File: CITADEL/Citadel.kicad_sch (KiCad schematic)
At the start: 33 parts, among them J1 Conn_01x02_Socket, J2 Conn_01x02_Socket, J3 USB3_A, J4 Conn_01x04_Socket, J5 Conn_01x03_Socket, J6 Conn_01x03_Socket, J7 Conn_01x03_Socket, J8 Conn_01x02_Pin, M1 Motor_DC, M2 Motor_DC, M3 Motor_DC, M4 Motor_DC, M5 Fan_Tacho, M6 Fan_Tacho, M7 Fan_Tacho, Q1 SSM3K329R_LF, Q2 SSM3K329R_LF, Q3 SSM3K329R_LF, Q4 SSM3K329R_LF, Q5 SSM3K329R_LF, Q6 SSM3K329R_LF, Q7 SSM3K329R_LF, U1 DEV-16771

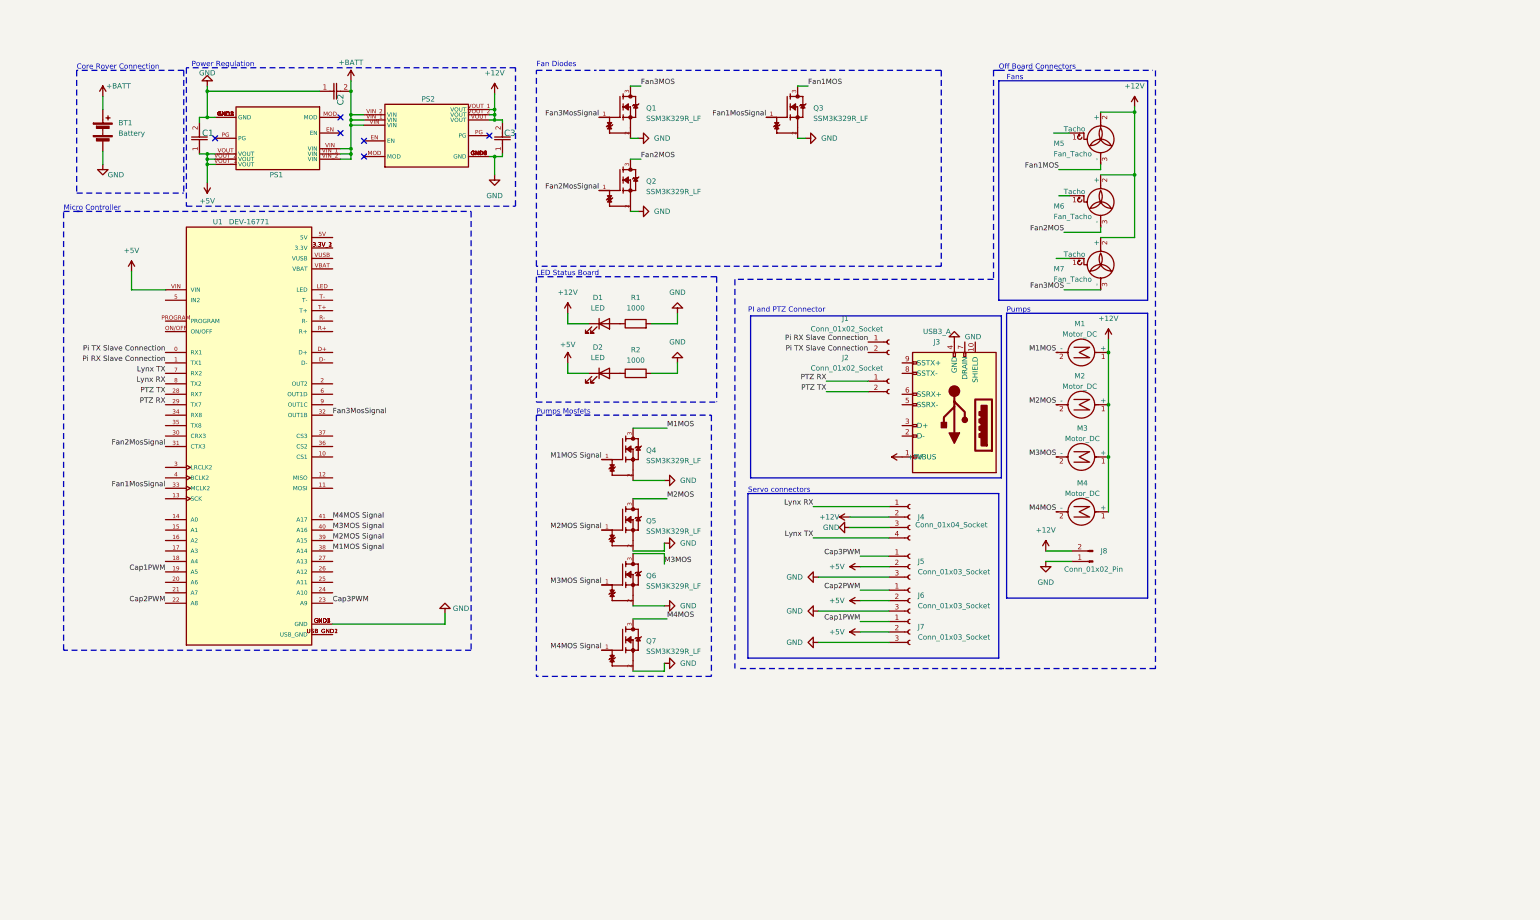
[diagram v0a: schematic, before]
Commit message: CITADEL 2025 V1, FAERIE 2025 V1
CITADEL January 27, 2025; FAERIE January 26, 2025; Katherine and Mason did CITADEL, Reymund did FAERIE
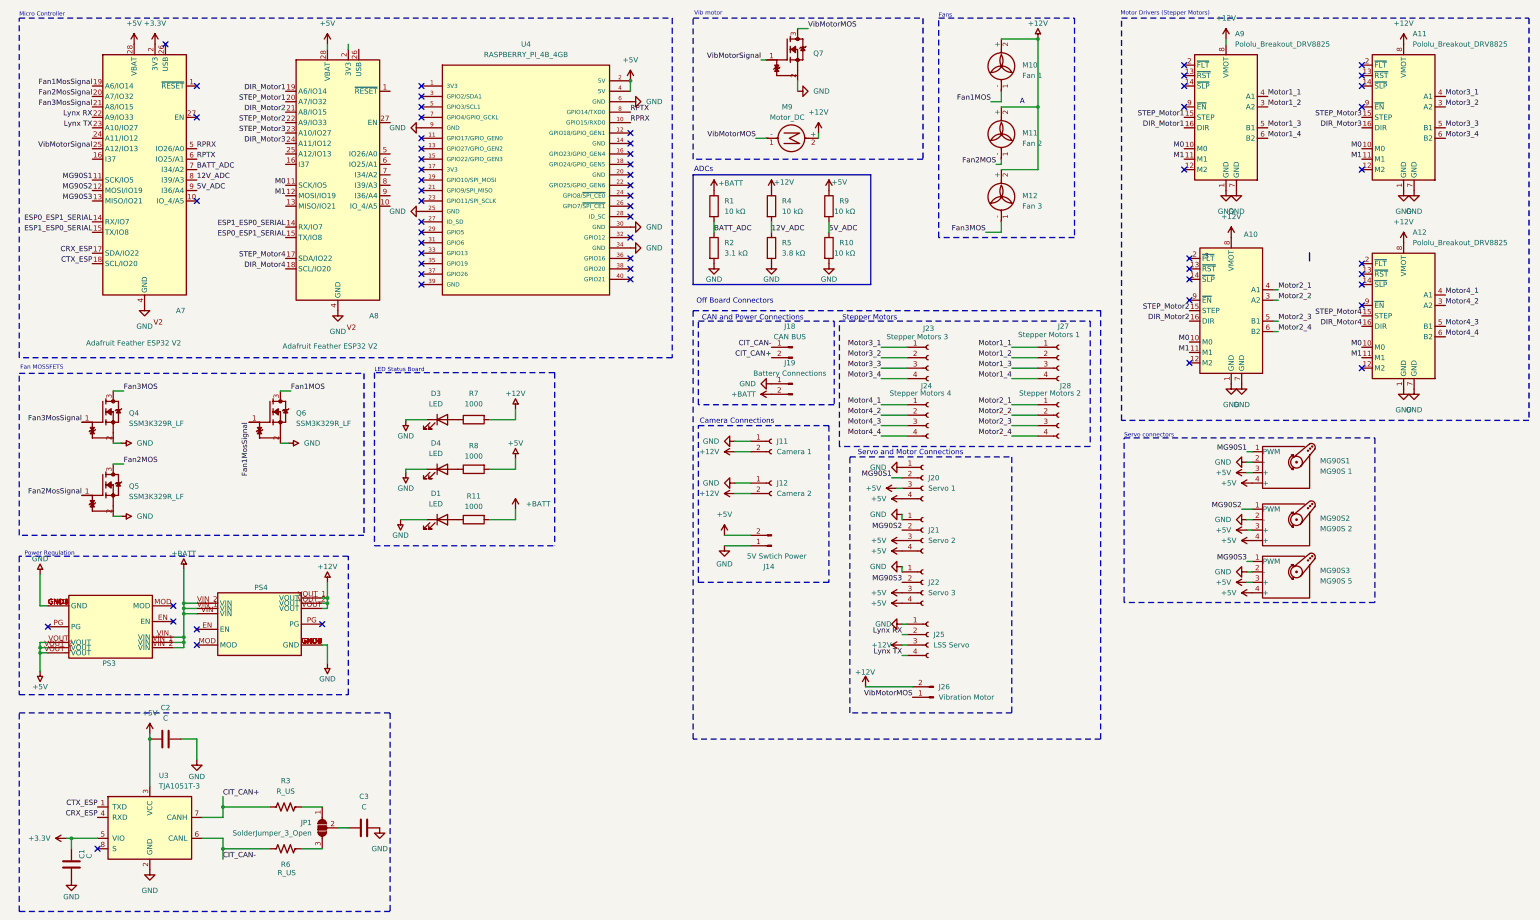
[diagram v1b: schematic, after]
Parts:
- removed BT1: Battery, Connector_AMASS:AMASS_XT60-F_1x02_P7.20mm_Vertical, symbol Device:Battery
- removed C1, C2, C3: 875105345011, Caps:CAP_WCAP-PSLP_6P3X7P7_WRE, symbol SMD Caps:875105345011
- removed D1, D2: LED, LED_SMD:LED_1210_3225Metric_Pad1.42x2.65mm_HandSolder, symbol Device:LED
- removed J1, J2: Conn_01x02_Socket, Connector_JST:JST_EH_B2B-EH-A_1x02_P2.50mm_Vertical, symbol Connector:Conn_01x02_Socket
- removed J3: USB3_A, Connector_USB:USB3_A_Molex_48393-001, symbol Connector:USB3_A
- removed J4: Conn_01x04_Socket, Connector_JST:JST_EH_B4B-EH-A_1x04_P2.50mm_Vertical, symbol Connector:Conn_01x04_Socket
- removed J5, J6, J7: Conn_01x03_Socket, Connector_JST:JST_EH_B3B-EH-A_1x03_P2.50mm_Vertical, symbol Connector:Conn_01x03_Socket
- removed J8: Conn_01x02_Pin, Connector_PinHeader_2.54mm:PinHeader_1x02_P2.54mm_Vertical, symbol Connector:Conn_01x02_Pin
- removed M1, M2, M3, M4: Motor_DC, Connector_JST:JST_EH_B2B-EH-A_1x02_P2.50mm_Vertical, symbol Motor:Motor_DC
- removed M5, M6, M7: Fan_Tacho, Connector_JST:JST_EH_B3B-EH-A_1x03_P2.50mm_Vertical, symbol Motor:Fan_Tacho
- removed PS1: ~, D24V150F5:D24V150F5, symbol Biosensor:Pololu_5V,_15A_Step-Down_Voltage_Regulator_D24V150F5
- removed PS2: ~, D24V150F5:D24V150F5, symbol Biosensor:Pololu_12V,_15A_Step-Down_Voltage_Regulator_D24V150F12
- removed Q1, Q2, Q3, Q4, Q5, Q6, Q7: SSM3K329R_LF, Nmos:SOTFL95P240X88-3N, symbol Nmos:SSM3K329R_LF
- removed U1: DEV-16771, Teensy:MODULE_DEV-16771, symbol Teensy:DEV-16771
- added A10, A11, A12, A9: Pololu_Breakout_DRV8825, Module:Pololu_Breakout-16_15.2x20.3mm, symbol Driver_Motor:Pololu_Breakout_DRV8825
- added A7, A8: Adafruit Feather ESP32 V2, Module:Adafruit_Feather, symbol Arm Force 3 Symbol Library:Adafruit_Feather_ESP32_V2
- added C1, C2, C3: C, Capacitor_SMD:C_0603_1608Metric_Pad1.08x0.95mm_HandSolder, symbol Device:C
- added D1, D3, D4: LED, LED_THT:LED_D3.0mm, symbol Citadel-altium-import:root_0_LED
- added J11: Camera 1, Connector_AMASS:AMASS_XT30U-F_1x02_P5.0mm_Vertical, symbol Connector:Conn_01x02_Socket
- added J12: Camera 2, Connector_AMASS:AMASS_XT30U-F_1x02_P5.0mm_Vertical, symbol Connector:Conn_01x02_Socket
- added J14: 5V Swtich Power, Connector_Molex:Molex_Mini-Fit_Jr_5566-02A_2x01_P4.20mm_Vertical, symbol Connector:Conn_01x02_Pin
- added J18: CAN BUS, Connector_AMASS:AMASS_XT30U-F_1x02_P5.0mm_Vertical, symbol Connector:Conn_01x02_Pin
- added J19: Battery Connections, Connector_AMASS:AMASS_XT60-M_1x02_P7.20mm_Vertical, symbol Connector:Conn_01x02_Pin
- added J20: Servo 1, Connector_Molex:Molex_Mini-Fit_Jr_5566-04A_2x02_P4.20mm_Vertical, symbol Connector:Conn_01x04_Socket
- added J21: Servo 2, Connector_Molex:Molex_Mini-Fit_Jr_5566-04A_2x02_P4.20mm_Vertical, symbol Connector:Conn_01x04_Socket
- added J22: Servo 3, Connector_Molex:Molex_Mini-Fit_Jr_5566-04A_2x02_P4.20mm_Vertical, symbol Connector:Conn_01x04_Socket
- added J23: Stepper Motors 3, Connector_Molex:Molex_Mini-Fit_Jr_5566-04A_2x02_P4.20mm_Vertical, symbol Connector:Conn_01x04_Socket
- added J24: Stepper Motors 4, Connector_Molex:Molex_Mini-Fit_Jr_5566-04A_2x02_P4.20mm_Vertical, symbol Connector:Conn_01x04_Socket
- added J25: LSS Servo, Connector_Molex:Molex_Mini-Fit_Jr_5566-04A_2x02_P4.20mm_Vertical, symbol Connector:Conn_01x04_Socket
- added J26: Vibration Motor, Connector_Molex:Molex_Mini-Fit_Jr_5566-02A_2x01_P4.20mm_Vertical, symbol Connector:Conn_01x02_Pin
- added J27: Stepper Motors 1, Connector_Molex:Molex_Mini-Fit_Jr_5566-04A_2x02_P4.20mm_Vertical, symbol Connector:Conn_01x04_Socket
- added J28: Stepper Motors 2, Connector_Molex:Molex_Mini-Fit_Jr_5566-04A_2x02_P4.20mm_Vertical, symbol Connector:Conn_01x04_Socket
- added JP1: SolderJumper_3_Open, Jumper:SolderJumper-3_P1.3mm_Open_Pad1.0x1.5mm, symbol Jumper:SolderJumper_3_Open
- added M10: Fan 1, Connector_Molex:Molex_Mini-Fit_Jr_5566-02A_2x01_P4.20mm_Vertical, symbol Motor:Fan
- added M11: Fan 2, Connector_Molex:Molex_Mini-Fit_Jr_5566-02A_2x01_P4.20mm_Vertical, symbol Motor:Fan
- added M12: Fan 3, Connector_Molex:Molex_Mini-Fit_Jr_5566-02A_2x01_P4.20mm_Vertical, symbol Motor:Fan
- added M9: Motor_DC, symbol Motor:Motor_DC
- added MG90S1: MG90S 1, symbol Motor:Motor_Servo
- added MG90S2: MG90S 2, symbol Motor:Motor_Servo
- added MG90S3: MG90S 5, symbol Motor:Motor_Servo
- added PS3: ~, Citadel:D24V15OF5, symbol Citadel-altium-import:root_2_Pololu_5V,_15A_Step-Down_Voltage_Regulator_D24V150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
- added PS4: ~, Citadel:D24V15OF5, symbol Citadel-altium-import:root_0_Pololu_12V,_15A_Step-Down_Voltage_Regulator_D24V15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
- added Q4, Q5, Q6: SSM3K329R_LF, Citadel:SSM3K329_LF, symbol Citadel-altium-import:root_0_SSM3K329R_LF
- added Q7: ~, Citadel:SSM3K329_LF, symbol Citadel-altium-import:root_0_SSM3K329R_LF
- added R10, R4, R9: 10 kΩ, Resistor_SMD:R_0603_1608Metric_Pad0.98x0.95mm_HandSolder, symbol Device:R
- added R11, R7, R8: 1000, Resistor_SMD:R_0603_1608Metric_Pad0.98x0.95mm_HandSolder, symbol Citadel-altium-import:root_1_R
- added R3, R6: R_US, Resistor_SMD:R_0603_1608Metric_Pad0.98x0.95mm_HandSolder, symbol Device:R_US
- added R5: 3.8 kΩ, Resistor_SMD:R_0603_1608Metric_Pad0.98x0.95mm_HandSolder, symbol Device:R
- added U3: TJA1051T-3, Package_SO:SOIC-8_3.9x4.9mm_P1.27mm, symbol Interface_CAN_LIN:TJA1051T-3
- added U4: RASPBERRY_PI_4B_4GB, Module:MODULE_RASPBERRY_PI_4B_4GB, symbol MCU_RaspberryPi_and_Boards:RASPBERRY_PI_4B_4GB
- R1: value 1000 -> 10 kΩ
- R2: value 1000 -> 3.1 kΩ
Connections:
- net +12V: now also A10.8 (VMOT), A11.8 (VMOT), A12.8 (VMOT), A9.8 (VMOT), J11.2 (Pin_2), J12.2 (Pin_2), J25.3 (Pin_3), J26.2 (Pin_2), M10.2 (+), M11.2 (+), M12.2 (+), M9.2 (+), PS4.VOUT, PS4.VOUT_1 (VOUT), PS4.VOUT_2 (VOUT), R4.1, R7.2
- net +5V: now also A7.28 (VBAT), A8.28 (VBAT), C2.2, J14.2 (Pin_2), J20.3 (Pin_3), J20.4 (Pin_4), J21.3 (Pin_3), J21.4 (Pin_4), J22.3 (Pin_3), J22.4 (Pin_4), MG90S1.3 (+), MG90S1.4 (+), MG90S2.3 (+), MG90S2.4 (+), MG90S3.3 (+), MG90S3.4 (+), PS3.VOUT, PS3.VOUT_1 (VOUT), PS3.VOUT_2 (VOUT), R8.2, R9.1, U3.3 (VCC), U4.2 (5V), U4.4 (5V)
- net +BATT: now also R1.1, J19.2 (Pin_2), PS3.VIN, PS3.VIN_1 (VIN), PS3.VIN_2 (VIN), PS4.VIN, PS4.VIN_1 (VIN), PS4.VIN_2 (VIN), R11.2
- net Fan1MOS: now also M10.1 (-), Q6.3
- net Fan1MosSignal: now also A7.19 (A6/IO14), Q6.1
- net Fan2MOS: now also M11.1 (-), Q5.3
- net Fan2MosSignal: now also A7.20 (A7/IO32), Q5.1
- net Fan3MOS: now also M12.1 (-), Q4.3
- net Fan3MosSignal: now also A7.21 (A8/IO15), Q4.1
- net GND: now also A10.1 (GND), A10.7 (GND), A11.1 (GND), A11.7 (GND), A12.1 (GND), A12.7 (GND), A7.4 (GND), A8.4 (GND), A9.1 (GND), A9.7 (GND), C1.2, C2.1, C3.1, D1.1 (K), D3.1 (K), D4.1 (K), J11.1 (Pin_1), J12.1 (Pin_1), J14.1 (Pin_1), J19.1 (Pin_1), J20.1 (Pin_1), J21.1 (Pin_1), J22.1 (Pin_1), J25.1 (Pin_1), MG90S1.2 (-), MG90S2.2 (-), MG90S3.2 (-), PS3.GND, PS3.GND1 (GND), PS3.GND2 (GND), PS3.GND3 (GND), PS3.GND4 (GND), PS3.GND5 (GND), PS3.GND6 (GND), PS3.GND7 (GND), PS4.GND, PS4.GND1 (GND), PS4.GND2 (GND), PS4.GND3 (GND), PS4.GND4 (GND), PS4.GND5 (GND), PS4.GND6 (GND), PS4.GND7 (GND), Q4.2, Q5.2, Q6.2, Q7.2, R10.2, R5.2, U3.2 (GND), U4.25 (GND), U4.30 (GND), U4.34 (GND), U4.6 (GND), U4.9 (GND); no longer R1.2
- net Lynx RX: now also A7.22 (A9/IO33), J25.2 (Pin_2)
- net Lynx TX: now also A7.23 (A10/IO27), J25.4 (Pin_4)
- net BATT_ADC: now reaches R2.1
- net BATT_ADC: now also R1.2, A7.7 (I34/A2)
- new net: D4.2 (A), R8.1
- new net: C3.2, JP1.2 (C)
- new net: JP1.1 (B), R3.1
- new net: JP1.3 (A), R6.1
- new net: D1.2 (A), R11.1
- new net: D3.2 (A), R7.1
- new net +3.3V: A7.2 (3V3), C1.1, U3.5 (VIO)
- new net 12V_ADC: A7.8 (I39/A3), R4.2, R5.1
- new net 5V_ADC: A7.9 (I36/A4), R10.1, R9.2
- new net CIT_CAN+: J18.2 (Pin_2), R3.2, U3.7 (CANH)
- new net CIT_CAN-: J18.1 (Pin_1), R6.2, U3.6 (CANL)
- new net CRX_ESP: A7.17 (SDA/IO22), U3.4 (RXD)
- new net CTX_ESP: A7.18 (SCL/IO20), U3.1 (TXD)
- new net DIR_Motor1: A8.19 (A6/IO14), A9.16 (DIR)
- new net DIR_Motor2: A10.16 (DIR), A8.21 (A8/IO15)
- new net DIR_Motor3: A11.16 (DIR), A8.24 (A11/IO12)
- new net DIR_Motor4: A12.16 (DIR), A8.18 (SCL/IO20)
- new net ESP0_ESP1_SERIAL: A7.14 (RX/IO7), A8.15 (TX/IO8)
- new net ESP1_ESP0_SERIAL: A7.15 (TX/IO8), A8.14 (RX/IO7)
- new net M0: A10.10 (M0), A11.10 (M0), A12.10 (M0), A8.11 (SCK/IO5), A9.10 (M0)
- new net M1: A10.11 (M1), A11.11 (M1), A12.11 (M1), A8.12 (MOSI/IO19), A9.11 (M1)
- new net MG90S1: A7.11 (SCK/IO5), J20.2 (Pin_2), MG90S1.1 (PWM)
- new net MG90S2: A7.12 (MOSI/IO19), J21.2 (Pin_2), MG90S2.1 (PWM)
- new net MG90S3: A7.13 (MISO/IO21), J22.2 (Pin_2), MG90S3.1 (PWM)
- new net Motor1_1: A9.4 (A1), J27.1 (Pin_1)
- new net Motor1_2: A9.3 (A2), J27.2 (Pin_2)
- new net Motor1_3: A9.5 (B1), J27.3 (Pin_3)
- new net Motor1_4: A9.6 (B2), J27.4 (Pin_4)
- new net Motor2_1: A10.4 (A1), J28.1 (Pin_1)
- new net Motor2_2: A10.3 (A2), J28.2 (Pin_2)
- new net Motor2_3: A10.5 (B1), J28.3 (Pin_3)
- new net Motor2_4: A10.6 (B2), J28.4 (Pin_4)
- new net Motor3_1: A11.4 (A1), J23.1 (Pin_1)
- new net Motor3_2: A11.3 (A2), J23.2 (Pin_2)
- new net Motor3_3: A11.5 (B1), J23.3 (Pin_3)
- new net Motor3_4: A11.6 (B2), J23.4 (Pin_4)
- new net Motor4_1: A12.4 (A1), J24.1 (Pin_1)
- new net Motor4_2: A12.3 (A2), J24.2 (Pin_2)
- new net Motor4_3: A12.5 (B1), J24.3 (Pin_3)
- new net Motor4_4: A12.6 (B2), J24.4 (Pin_4)
- new net RPRX: A7.5 (IO26/A0), U4.10 (GPIO15/RXD0)
- new net RPTX: A7.6 (IO25/A1), U4.8 (GPIO14/TXD0)
- new net STEP_Motor1: A8.20 (A7/IO32), A9.15 (STEP)
- new net STEP_Motor2: A10.15 (STEP), A8.22 (A9/IO33)
- new net STEP_Motor3: A11.15 (STEP), A8.23 (A10/IO27)
- new net STEP_Motor4: A12.15 (STEP), A8.17 (SDA/IO22)
- new net VibMotorMOS: J26.1 (Pin_1), M9.1 (-), Q7.3
- new net VibMotorSignal: A7.25 (A12/IO13), Q7.1
- no-connect marks 6 -> 62
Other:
- note added: "3"
- note added: "A"
- note added: "ADCs"
- note added: "CAN and Power Connections"
- note added: "Camera Connections"
- note added: "Fan MOSSFETS"
- note added: "Motor Drivers (Stepper Motors)"
- note added: "Servo and Motor Connections"
- note added: "Stepper Motors"
- note added: "Vib motor"
- note removed: "Core Rover Connection"
- note removed: "Fan Diodes"
- note removed: "PI and PTZ Connector"
- note removed: "Pumps"
- note removed: "Pumps Mosfets"

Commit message: CITADEL 2025 V2
April 8, 2025; replaced the second MCU with a GPIO extender IC that didn't end up working
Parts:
- removed A7, A8: Adafruit Feather ESP32 V2, Module:Adafruit_Feather, symbol Arm Force 3 Symbol Library:Adafruit_Feather_ESP32_V2
- added C4: 0.047uF, Capacitor_SMD:C_0603_1608Metric_Pad1.08x0.95mm_HandSolder, symbol Device:C
- added U1: MAX7315AUE_T, Citadel:MAX7315AUE+T, symbol Citadel-altium-import:MAX7315AUE_T
- added U2: ~, Citadel:esp32_devkit_v1, symbol ESP 32 DOIT devkit V1:ESP32_DOIT_devkit_V1
- Q7: value ~ -> SSM3K329R_LF; ALTIUM_VALUE (none) -> SSM3K329R_LF; AVAILABILITY (none) -> In Stock; CHECK_PRICES (none) -> https://www.snapeda.com/parts/SSM3K329R,LF/Toshiba+Semicond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; DESCRIPTION (none) -> \nN-Channel 30 V 3.5A (Ta) 1W (Ta) Surface Mount SOT-23~{F}n; FOOTPRINT (none) -> Nmos:SOTFL95P240X88-3N; MANUFACTURER (none) -> Toshiba; MAXIMUM_PACKAGE_HEIGHT (none) -> 0.88mm; MF (none) -> Toshiba Semiconductor; MP (none) -> SSM3K329R,LF; PACKAGE (none) -> SOT-23 Toshiba; PARTREV (none) -> 1.0; PRICE (none) -> None; PURCHASE-URL (none) -> https://www.snapeda.com/api/url_track_click_mouser/?unipart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; SNAPEDA_LINK (none) -> https://www.snapeda.com/parts/SSM3K329R,LF/Toshiba+Semicond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; SNAPEDA_PN (none) -> SSM3K329R,LF; STANDARD (none) -> IPC-7351B
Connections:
- net DIR_Motor2 is gone; now on net DIR: A10.16 (DIR)
- net DIR_Motor3 is gone; now on net DIR: A11.16 (DIR)
- net DIR_Motor4 is gone; now on net DIR: A12.16 (DIR)
- net +12V: now also M9.1 (+); no longer M9.2 (+)
- net +3.3V: now also C4.2, U1.16 (V+), U2.16 (3.3V)
- net +5V: now also U2.15 (VIN)
- net 12V_ADC: now also U2.3 (GPI39/A3)
- net 5V_ADC: now also U2.4 (GPI34/A6)
- net BATT_ADC: now also U2.2 (GPI36/A0)
- net CRX_ESP: now also U2.11 (GPIO14/A16)
- net CTX_ESP: now also U2.13 (GPIO13/A14)
- net Fan1MosSignal: now also U1.10 (P5)
- net Fan2MosSignal: now also U1.11 (P6)
- net Fan3MosSignal: now also U1.12 (P7)
- net GND: now also C4.1, U1.1 (AD0), U1.2 (AD1), U1.3 (AD2), U1.8 (GND), U2.14 (GND), U2.17 (GND)
- net Lynx RX: now also U2.21 (GPIO16/RX2)
- net Lynx TX: now also U2.22 (GPIO17/TX2)
- net M0: now also U2.24 (GPIO18/SCK)
- net M1: now also U2.30 (GPIO23/MOSI)
- net MG90S1: now also U1.7 (P3)
- net MG90S2: now also U1.6 (P2)
- net MG90S3: now also U1.5 (P1)
- net STEP_Motor1: now also U2.8 (GPIO25/A18)
- net STEP_Motor2: now also U2.6 (GPIO32/A4)
- net STEP_Motor3: now also U2.20 (GPIO4/A10)
- net STEP_Motor4: now also U2.25 (GPIO19/MISO)
- net VibMotorMOS: now also M9.2 (-); no longer M9.1 (-)
- net VibMotorSignal: now also U1.4 (P0)
- net Step_Motor_Enable: now reaches A12.9 (~{EN})
- net Step_Motor_Enable: now also A10.9 (~{EN}), A11.9 (~{EN}), A9.9 (~{EN}), U1.9 (P4)
- net DIR_Motor1 renamed DIR
- net DIR: now also U2.7 (GPIO33/A5)
- net RPRX renamed RASPI_TX
- net RASPI_TX: now also U2.10 (GPIO27/A17)
- net RPTX renamed RASPI_RX
- net RASPI_RX: now also U2.9 (GPIO26/A19)
- new net MAX_SCL: U1.14 (SCL), U2.29 (GPIO22/SCL)
- new net MAX_SDA: U1.15 (SDA), U2.26 (GPIO21/SDA)
- no-connect marks 62 -> 63
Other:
- moved on the sheet: A10, A11, A12, A9, J11, J12, J14, J18, J19, J20, J21, J22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

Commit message: CITADEL 2025 V3
May 11, 2025; got rid of the GPIO extender
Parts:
- removed C4: 0.047uF, Capacitor_SMD:C_0603_1608Metric_Pad1.08x0.95mm_HandSolder, symbol Device:C
- removed U1: MAX7315AUE_T, Citadel:MAX7315AUE+T, symbol Citadel-altium-import:MAX7315AUE_T
- added JP2, JP3, JP4, JP5: SolderJumper_3_Open, Jumper:SolderJumper-3_P1.3mm_Open_Pad1.0x1.5mm, symbol Jumper:SolderJumper_3_Open
- R2: value 3.1 kΩ -> 2.21 kΩ
- R5: value 3.8 kΩ -> 3.32 kΩ
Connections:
- net MAX_SCL is gone; now on net Fan2MosSignal: U2.29 (GPIO22/SCL)
- net MAX_SDA is gone; now on net Fan3MosSignal: U2.26 (GPIO21/SDA)
- net +3.3V: now also JP2.1 (B), JP3.1 (B)
- net Fan1MosSignal: now also U2.30 (GPIO23/MOSI)
- net GND: now also JP2.3 (A), JP3.3 (A)
- net M0: now also JP2.2 (C); no longer U2.24 (GPIO18/SCK)
- net M1: now also JP3.2 (C); no longer U2.30 (GPIO23/MOSI)
- net MG90S1: now also U2.9 (GPIO26/A19), JP4.1 (B), JP5.1 (B)
- net MG90S2: now also JP5.2 (C)
- net MG90S3: now also JP4.2 (C)
- net Step_Motor_Enable: now also U2.10 (GPIO27/A17)
- net VibMotorSignal: now also U2.24 (GPIO18/SCK)
- net MG90S3_T: now reaches U2.18 (GPIO15/A13)
- net MG90S3_T: now also JP4.3 (A)
- net MG90S2_T: now reaches U2.23 (GPIO05/CS)
- net MG90S2_T: now also JP5.3 (A)
- net RASPI_RX: no longer names the net of U4.8 (GPIO14/TXD0)
- net RASPI_RX: no longer U2.9 (GPIO26/A19)
- net RASPI_TX: no longer names the net of U4.10 (GPIO15/RXD0)
- net RASPI_TX: no longer U2.10 (GPIO27/A17)
- no-connect marks 63 -> 62
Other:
- moved on the sheet: U2
